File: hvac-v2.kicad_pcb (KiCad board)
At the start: 2 copper layers, 114 x 60 mm, 37 parts, among them J1 Conn_01x04, J2 Anderson_two_redblack, J3 Anderson_two_redblack, J4 Anderson_two_redblack, P1 10118194, P2 CONN_01X08, SW1 SW_SPST, SW3 KS-01Q-01, SW4 KS-01Q-01, SW5 SPST, U1 SAMD21E18, U2 WS2812b, U3 MIC5203, U4 MOSFET_CSD17318Q2, U5 WS2812b, U6 WS2812b, U7 MOSFET_CSD17318Q2, U8 DS18B20

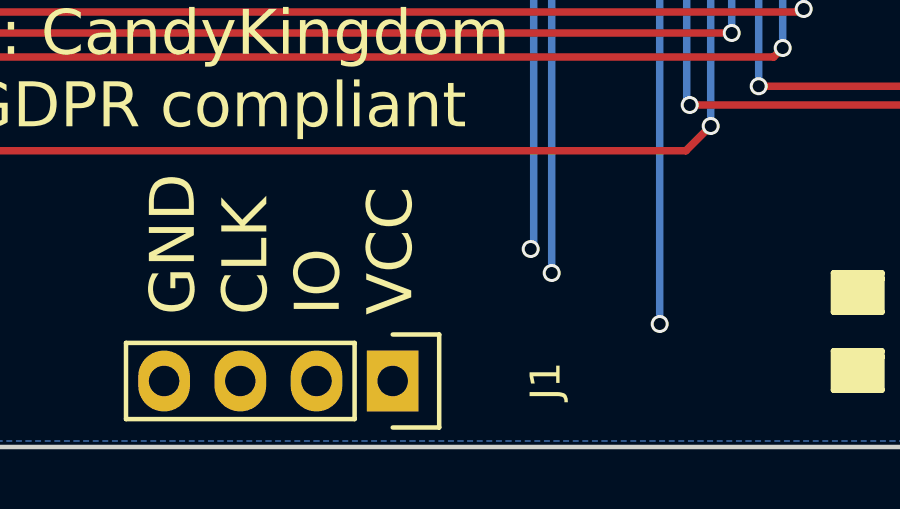
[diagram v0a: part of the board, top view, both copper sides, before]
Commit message: Connect programming headers
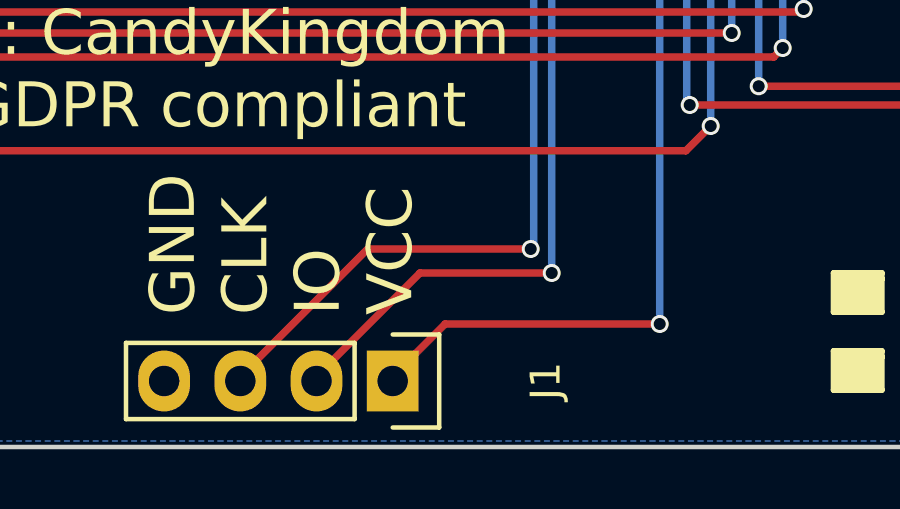
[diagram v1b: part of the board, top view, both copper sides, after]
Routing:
- net ARM_SWCLK: track 27.2 -> 38.8 mm
- net VCC: track 405.2 -> 415.0 mm
- net ARM_SWDIO: track 24.9 -> 34.3 mm
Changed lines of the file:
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@@
     (links 96)
     (no_connects 0)
-    (area 45.924999 43.924999 160.075001 104.075001)
+    (area 44.036499 35.224999 160.075001 104.075001)
     (thickness 1.6)
     (drawings 89)
-    (tracks 501)
+    (tracks 510)
     (zones 0)
     (modules 37)
@@
   (page A4)
   (layers
-    (0 F.Cu signal hide)
-    (31 B.Cu signal hide)
-    (32 B.Adhes user hide)
-    (33 F.Adhes user hide)
-    (34 B.Paste user hide)
-    (35 F.Paste user hide)
-    (36 B.SilkS user hide)
+    (0 F.Cu signal)
+    (31 B.Cu signal)
+    (32 B.Adhes user)
+    (33 F.Adhes user)
+    (34 B.Paste user)
+    (35 F.Paste user)
+    (36 B.SilkS user)
     (37 F.SilkS user)
     (38 B.Mask user)
@@
     (effects (font (size 1.5 1.5) (thickness 0.3)))
   )
-  (gr_text "TINY DIODE" (at 61.2 83.8 360) (layer F.Fab)
+  (gr_text "TINY DIODE" (at 61.2 83.8) (layer F.Fab)
     (effects (font (size 1.5 1.5) (thickness 0.3)))
   )
@@
   (segment (start 139.49 68) (end 134.89 72.6) (width 5) (layer F.Cu) (net 2))
   (segment (start 113.954002 72.6) (end 108.754002 67.4) (width 5) (layer F.Cu) (net 2))
+  (segment (start 121 99.9) (end 113.8476 99.9) (width 0.25) (layer F.Cu) (net 3))
+  (segment (start 113.8476 99.9) (end 112.1 101.6476) (width 0.25) (layer F.Cu) (net 3))
+  (segment (start 112.1 101.6476) (end 112.1 101.8) (width 0.25) (layer F.Cu) (net 3))
   (segment (start 122.275736 75.7) (end 122.7 75.7) (width 0.25) (layer F.Cu) (net 3))
   (segment (start 122.250734 75.674998) (end 122.275736 75.7) (width 0.25) (layer F.Cu) (net 3))
@@
   (segment (start 141.76 97.26) (end 141.7 97.2) (width 0.25) (layer F.Cu) (net 31))
   (via (at 141.7 97.2) (size 0.6) (drill 0.4) (layers F.Cu B.Cu) (net 31))
+  (segment (start 116.7 97.4) (end 111.2676 97.4) (width 0.25) (layer F.Cu) (net 39))
+  (segment (start 111.2676 97.4) (end 107.02 101.6476) (width 0.25) (layer F.Cu) (net 39))
+  (segment (start 107.02 101.6476) (end 107.02 101.8) (width 0.25) (layer F.Cu) (net 39))
   (segment (start 116.8 76.3) (end 116.8 97.3) (width 0.25) (layer B.Cu) (net 39))
   (segment (start 116.8 97.3) (end 116.7 97.4) (width 0.25) (layer B.Cu) (net 39))
@@
   (segment (start 116.852601 76.247399) (end 116.8 76.3) (width 0.25) (layer F.Cu) (net 39))
   (via (at 116.8 76.3) (size 0.6) (drill 0.4) (layers F.Cu B.Cu) (net 39))
+  (segment (start 117.4 98.2) (end 113.0076 98.2) (width 0.25) (layer F.Cu) (net 40))
+  (segment (start 113.0076 98.2) (end 109.56 101.6476) (width 0.25) (layer F.Cu) (net 40))
+  (segment (start 109.56 101.6476) (end 109.56 101.8) (width 0.25) (layer F.Cu) (net 40))
   (segment (start 117.5 77) (end 120.89352 77) (width 0.25) (layer F.Cu) (net 40))
   (segment (start 120.89352 77) (end 121.10092 77.2074) (width 0.25) (layer F.Cu) (net 40))

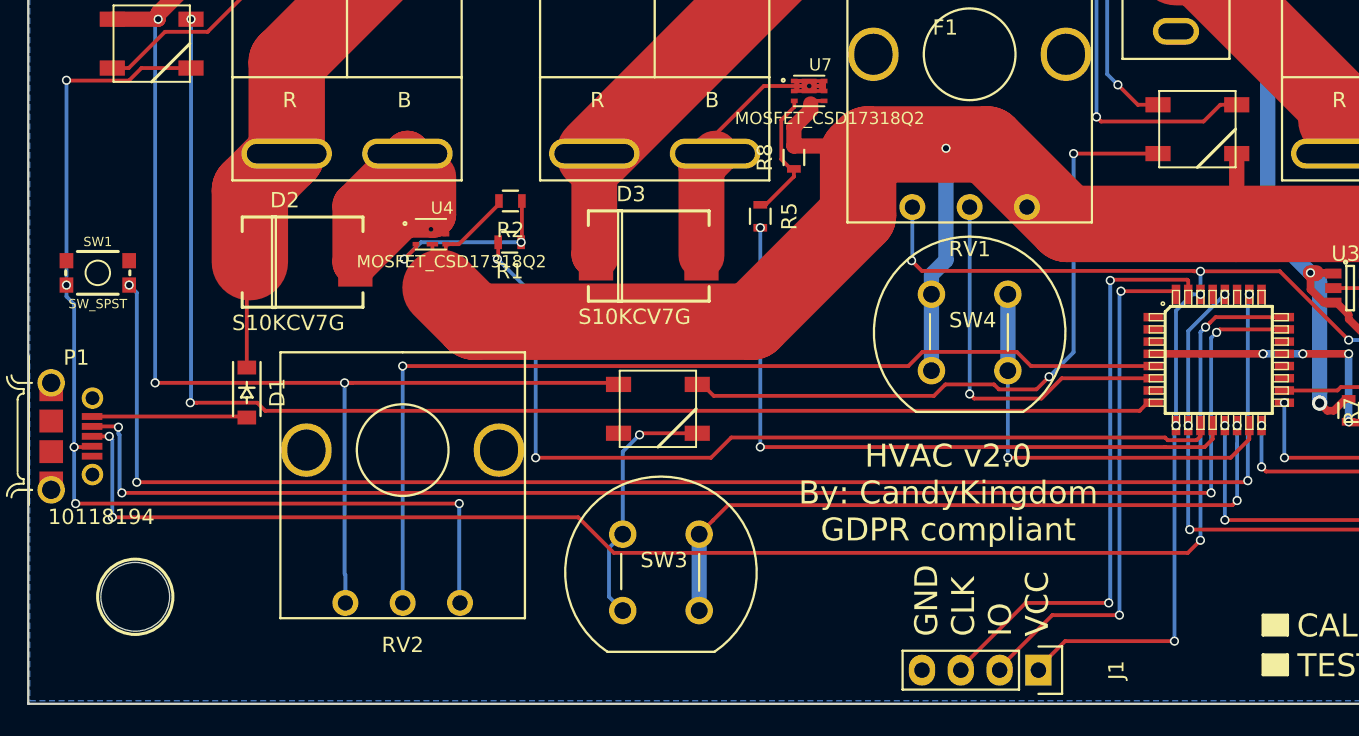
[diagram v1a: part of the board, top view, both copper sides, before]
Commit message: Hardware revision 2.1: - Fix SWD connection to power to not connect directly to VCC - Add silk labels for controls
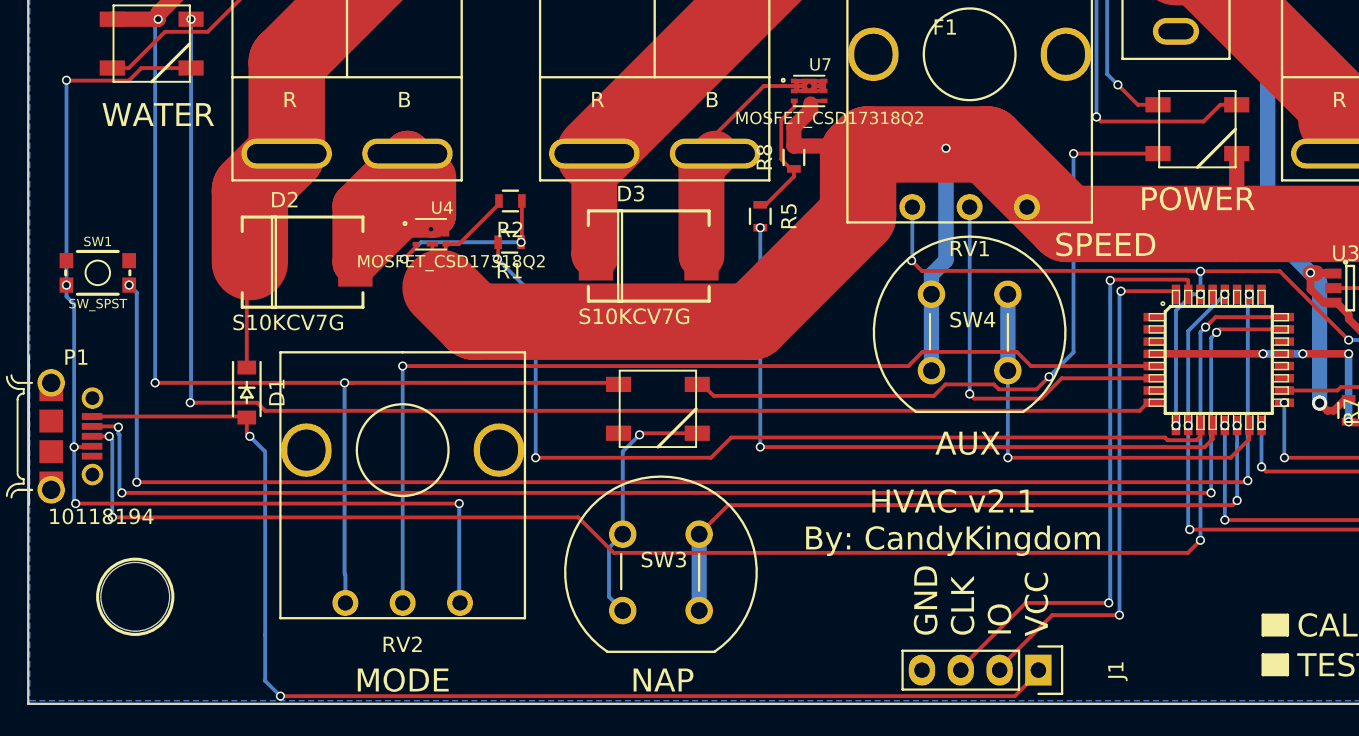
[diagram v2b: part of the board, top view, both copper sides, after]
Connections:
- D1 pad 2: Net-(D1-Pad2) -> USB_VCC
- J1 pad 1: VCC -> USB_VCC
- P1 pad 1: Net-(D1-Pad2) -> USB_VCC
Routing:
- net USB_VCC: track 0.00 -> 79.8 mm, vias 0 -> 2
- net VCC: track 415.0 -> 391.2 mm, vias 16 -> 15
- net Net-(D1-Pad2): track 10.2 -> 0.00 mm
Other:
- board text added: "AUX"
- board text added: "HVAC v2.1 By: CandyKingdom"
- board text added: "MODE"
- board text added: "NAP"
- board text added: "POWER"
- board text added: "SPEED"
- board text added: "WATER"
- board text removed: "HVAC v2.0 By: CandyKingdom GDPR compliant"

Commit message: Start placing components
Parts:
- removed P1: 10118194, 10118194-0001LF:FRAMATOME_10118194-0001LF
- removed P2: CONN_01X08, homebrew:1985250_phoenix_8pos_3.5mm
- removed RV1, RV2: POT, homebrew:BOURNS_PDB12H_POT
- removed SW3, SW4: KS-01Q-01, homebrew:BUTTON_KS-01Q-01
- removed SW5: SPST, homebrew:SWITCH_100SP1T2B3M1QEH
- removed U6: WS2812b, homebrew:WS2812B
- removed U7: MOSFET_CSD17318Q2, homebrew:TRANS_CSD17318Q2T
- removed U8: DS18B20, homebrew:TO-92
- added BZ1: Buzzer, homebrew:MURATA_PKM13EPYH4000-A0, F.Cu at (250.1, 137.4)
- added C10: 0.22uF, Capacitor_SMD:C_0805_2012Metric, F.Cu at (207.4, 189.2)
- added C11: 0.22uF, Capacitor_SMD:C_0805_2012Metric, F.Cu at (249.5, 146.0)
- added C12: 0.1uF, Capacitor_SMD:C_0402_1005Metric, F.Cu at (290.4, 148.9)
- added C13: 0.1uF, Capacitor_SMD:C_0402_1005Metric, F.Cu at (266.6, 172.8)
- added C14: 4.7uF, Capacitor_SMD:C_0603_1608Metric, F.Cu at (224.5, 190.8)
- added C15: 0.22uF, Capacitor_SMD:C_0805_2012Metric, F.Cu at (211.5, 172.8)
- added C16: 0.22uF, Capacitor_SMD:C_0805_2012Metric, F.Cu at (203.0, 189.2)
- added C17: 0.1uF, Capacitor_SMD:C_0402_1005Metric, F.Cu at (249.8, 186.7)
- added C18: 0.1uF, Capacitor_SMD:C_0402_1005Metric, F.Cu at (273.8, 165.5)
- added C19: 1000uF, Capacitor_THT:CP_Radial_D10.0mm_P5.00mm, F.Cu at (250.1, 162.4)
- added C20: 1nF, Capacitor_SMD:C_0402_1005Metric, F.Cu at (280.5, 156.1)
- added C21: 0.1uF, Capacitor_SMD:C_0402_1005Metric, F.Cu at (262.4, 175.9)
- added C22: 0.1uF, Capacitor_SMD:C_0402_1005Metric, F.Cu at (256.7, 181.8)
- added C23: 0.1uF, Capacitor_SMD:C_0402_1005Metric, F.Cu at (249.8, 188.7)
- added C24: 0.1uF, Capacitor_SMD:C_0402_1005Metric, F.Cu at (269.8, 168.9)
- added C25: 0.1uF, Capacitor_SMD:C_0402_1005Metric, F.Cu at (266.6, 170.9)
- added C26: 0.1uF, Capacitor_SMD:C_0402_1005Metric, F.Cu at (290.4, 146.9)
- added C27: 0.1uF, Capacitor_SMD:C_0402_1005Metric, F.Cu at (258.1, 178.8)
- added C28: 0.1uF, Capacitor_SMD:C_0402_1005Metric, F.Cu at (275.7, 161.6)
- added C29: 0.1uF, Capacitor_SMD:C_0402_1005Metric, F.Cu at (226.8, 157.6)
- added C30: 0.1uF, Capacitor_SMD:C_0402_1005Metric, F.Cu at (286.2, 151.9)
- added C31: 0.1uF, Capacitor_SMD:C_0402_1005Metric, F.Cu at (280.5, 158.1)
- added C32: 0.1uF, Capacitor_SMD:C_0402_1005Metric, F.Cu at (283.4, 156.1)
- added C33: 0.1uF, Capacitor_SMD:C_0402_1005Metric, F.Cu at (207.5, 172.3)
- added C34: 0.1uF, Capacitor_SMD:C_0402_1005Metric, F.Cu at (229.6, 157.6)
- added C35: 0.1uF, Capacitor_SMD:C_0402_1005Metric, F.Cu at (272.0, 131.8)
- added C36: 0.1uF, Capacitor_SMD:C_0402_1005Metric, F.Cu at (270.0, 161.6)
- added C37: 0.1uF, Capacitor_SMD:C_0402_1005Metric, F.Cu at (272.8, 161.6)
- added C38: 4.7uF, Capacitor_SMD:C_0603_1608Metric, F.Cu at (200.0, 172.6)
- added C39: 1000uF, Capacitor_THT:CP_Radial_D10.0mm_P5.00mm, F.Cu at (226.2, 183.8)
- added C4: 0.1uF, Capacitor_SMD:C_0402_1005Metric, F.Cu at (276.7, 163.5)
- added C40: 0.1uF, Capacitor_SMD:C_0402_1005Metric, F.Cu at (253.8, 181.8)
- added C41: 0.1uF, Capacitor_SMD:C_0402_1005Metric, F.Cu at (249.8, 184.8)
- added C42: 0.1uF, Capacitor_SMD:C_0402_1005Metric, F.Cu at (273.8, 163.5)
- added C43: 0.1uF, Capacitor_SMD:C_0402_1005Metric, F.Cu at (252.7, 184.8)
- added C5: 0.1uF, Capacitor_SMD:C_0402_1005Metric, F.Cu at (294.4, 144.0)
- added C6: 0.1uF, Capacitor_SMD:C_0402_1005Metric, F.Cu at (252.7, 186.7)
- added C7: 0.1uF, Capacitor_SMD:C_0402_1005Metric, F.Cu at (278.6, 160.8)
- added C8: 0.1uF, Capacitor_SMD:C_0402_1005Metric, F.Cu at (260.9, 178.8)
- added C9: 4.7uF, Capacitor_SMD:C_0603_1608Metric, F.Cu at (254.1, 155.2)
- added D10: TVS_5V, Diode_SMD:D_SOD-323, F.Cu at (254.8, 172.6)
- added D11: TVS_5V, Diode_SMD:D_SOD-323, F.Cu at (282.9, 146.1)
- added D12: TVS_5V, Diode_SMD:D_SOD-323, F.Cu at (254.8, 169.7)
- added D13: TVS_5V, Diode_SMD:D_SOD-323, F.Cu at (236.6, 188.1)
- added D14: TVS_5V, Diode_SMD:D_SOD-323, F.Cu at (293.6, 130.6)
- added D15: TVS_5V, Diode_SMD:D_SOD-323, F.Cu at (254.3, 149.5)
- added D16: D_Schottky, Diode_THT:D_DO-201AD_P12.70mm_Horizontal, F.Cu at (218.1, 162.3)
- added D17: D_Schottky, Diode_THT:D_DO-201AD_P12.70mm_Horizontal, F.Cu at (194.2, 184.1)
- added D18: D_Schottky, Diode_THT:D_DO-201AD_P12.70mm_Horizontal, F.Cu at (227.7, 146.1)
- added D19: TVS_5V, Diode_SMD:D_SOD-323, F.Cu at (216.1, 189.2)
- added D20: TVS_5V, Diode_SMD:D_SOD-323, F.Cu at (246.5, 179.8)
- added D21: TVS_5V, Diode_SMD:D_SOD-323, F.Cu at (294.2, 133.6)
- added D22: TVS_5V, Diode_SMD:D_SOD-323, F.Cu at (240.9, 188.1)
- added D23: TVS_5V, Diode_SMD:D_SOD-323, F.Cu at (220.4, 189.2)
- added D24: TVS_5V, Diode_SMD:D_SOD-323, F.Cu at (254.3, 152.4)
- added D4: TVS_12V, Diode_SMD:D_SMB_Handsoldering, F.Cu at (292.5, 126.3)
- added D5: LED, LED_SMD:LED_0805_2012Metric, F.Cu at (211.5, 175.9)
- added D6: TVS_5V, Diode_SMD:D_SOD-323, F.Cu at (294.2, 136.5)
- added D7: TVS_5V, Diode_SMD:D_SOD-323, F.Cu at (259.1, 171.3)
- added D8: D_Schottky, Diode_THT:D_DO-201AD_P12.70mm_Horizontal, F.Cu at (171.5, 62.6)
- added D9: D_Schottky, Diode_THT:D_DO-201AD_P12.70mm_Horizontal, F.Cu at (171.5, 56.3)
- added J10: Conn_01x02, Connector_PinHeader_2.54mm:PinHeader_1x02_P2.54mm_Horizontal, F.Cu at (90.1, 97.6)
- added J11: Conn_01x03, Connector_PinHeader_2.54mm:PinHeader_1x03_P2.54mm_Horizontal, F.Cu at (89.9, 78.1)
- added J12: Conn_01x03, Connector_PinHeader_2.54mm:PinHeader_1x03_P2.54mm_Horizontal, F.Cu at (90.1, 89.4)
- added J13: Conn_01x03, Connector_PinHeader_2.54mm:PinHeader_1x03_P2.54mm_Horizontal, F.Cu at (90.0, 118.0)
- added J14: Conn_01x04, Connector_PinHeader_2.54mm:PinHeader_1x04_P2.54mm_Horizontal, F.Cu at (259.5, 142.8)
- added J5: Conn_01x03, Connector_PinHeader_2.54mm:PinHeader_1x03_P2.54mm_Horizontal, F.Cu at (89.9, 107.4)
- added J6: Conn_01x03, Connector_PinHeader_2.54mm:PinHeader_1x03_P2.54mm_Horizontal, F.Cu at (259.5, 133.1)
- added J7: Anderson_two_redblack_sink, homebrew:Anderson_1336G1_right_angle_bottom_two, F.Cu at (114.1, 51.1)
- added J8: Anderson_two_redblack_sink, homebrew:Anderson_1336G1_right_angle_bottom_two, F.Cu at (93.8, 51.4)
- added J9: Conn_01x02, Connector_PinHeader_2.54mm:PinHeader_1x02_P2.54mm_Horizontal, F.Cu at (90.1, 67.0)
- added JP1: SolderJumper_2_Open, Jumper:SolderJumper-2_P1.3mm_Open_TrianglePad1.0x1.5mm, F.Cu at (254.3, 146.2)
- added JP2: SolderJumper_2_Open, Jumper:SolderJumper-2_P1.3mm_Open_TrianglePad1.0x1.5mm, F.Cu at (211.8, 189.4)
- added Q1: AO3400A, Package_TO_SOT_SMD:SOT-23, F.Cu at (245.0, 146.8)
- added Q2: AO3400A, Package_TO_SOT_SMD:SOT-23, F.Cu at (198.5, 189.8)
- added Q3: AO3400A, Package_TO_SOT_SMD:SOT-23, F.Cu at (194.1, 189.8)
- added R10: 10k, Resistor_SMD:R_0603_1608Metric, F.Cu at (232.5, 190.8)
- added R11: 10k, Resistor_SMD:R_0603_1608Metric, F.Cu at (294.1, 139.2)
- added R12: 10k, Resistor_SMD:R_0603_1608Metric, F.Cu at (263.2, 171.1)
- added R13: 150, Resistor_SMD:R_0603_1608Metric, F.Cu at (287.0, 144.7)
- added R14: 470, Resistor_SMD:R_0603_1608Metric, F.Cu at (282.7, 148.8)
- added R15: 150, Resistor_SMD:R_0603_1608Metric, F.Cu at (277.1, 156.0)
- added R16: 47, Resistor_SMD:R_0603_1608Metric, F.Cu at (282.7, 151.3)
- added R17: 10k, Resistor_SMD:R_0603_1608Metric, F.Cu at (287.0, 147.2)
- added R18: 10k, Resistor_SMD:R_0603_1608Metric, F.Cu at (270.4, 166.6)
- added R19: 10k, Resistor_SMD:R_0603_1608Metric, F.Cu at (240.5, 190.8)
- added R20: 10k, Resistor_SMD:R_0603_1608Metric, F.Cu at (291.0, 144.7)
- added R21: 24k, Resistor_SMD:R_0603_1608Metric, F.Cu at (246.3, 187.6)
- added R22: 24k, Resistor_SMD:R_0603_1608Metric, F.Cu at (254.6, 179.6)
- added R23: 150, Resistor_SMD:R_0603_1608Metric, F.Cu at (246.3, 185.0)
- added R24: 150, Resistor_SMD:R_0603_1608Metric, F.Cu at (250.4, 182.5)
- added R25: 4k7, Resistor_SMD:R_0603_1608Metric, F.Cu at (270.4, 164.1)
- added R26: 4k7, Resistor_SMD:R_0603_1608Metric, F.Cu at (246.3, 182.5)
- added R27: 4k7, Resistor_SMD:R_0603_1608Metric, F.Cu at (286.7, 149.7)
- added R28: 4k7, Resistor_SMD:R_0603_1608Metric, F.Cu at (282.7, 153.8)
- added R3: 10k, Resistor_SMD:R_0603_1608Metric, F.Cu at (244.5, 190.8)
- added R4: 10k, Resistor_SMD:R_0603_1608Metric, F.Cu at (228.5, 190.8)
- added R9: 110k, Resistor_SMD:R_0603_1608Metric, F.Cu at (250.6, 179.6)
- added SW2: Rotary_Encoder_Switch, homebrew:BOURNS_PEC12R-4xxxF-Sxxxx, F.Cu at (183.8, 182.9)
- C1: value 10uF -> 4.7uF; footprint Capacitors_SMD:C_0805 -> Capacitor_SMD:C_0603_1608Metric
- C2: value 1uF -> 0.1uF; footprint Capacitors_SMD:C_0603 -> Capacitor_SMD:C_0402_1005Metric
- C3: value 1uF -> 1nF; footprint Capacitors_SMD:C_0603 -> Capacitor_SMD:C_0402_1005Metric
- D1: value BAT54GWJ -> TVS_5V; footprint Diodes_SMD:SOD-123 -> Diode_SMD:D_SOD-323
- D2: value S10KCV7G -> TVS_5V; footprint homebrew:DIODE-DO-214AB -> Diode_SMD:D_SOD-323
- D3: value S10KCV7G -> D_Schottky; footprint homebrew:DIODE-DO-214AB -> Diode_THT:D_DO-201AD_P12.70mm_Horizontal
- F1: footprint homebrew:FUSEHOLDER_ATC_Bk-6010 -> homebrew:FUSE_3550-2
- J1: value Conn_01x04 -> Anderson_two_redblack; footprint Pin_Headers:Pin_Header_Straight_1x04 -> homebrew:Anderson_1336G1_right_angle_bottom_two
- J2: value Anderson_two_redblack -> Conn_01x04; footprint homebrew:Anderson_1337G3_right_angle_bottom_two -> Connector_PinHeader_2.54mm:PinHeader_1x04_P2.54mm_Horizontal
- J3: value Anderson_two_redblack -> Conn_01x02; footprint homebrew:Anderson_1337G3_right_angle_bottom_two -> Connector_PinHeader_2.54mm:PinHeader_1x02_P2.54mm_Horizontal
- J4: value Anderson_two_redblack -> Anderson_two_redblack_src; footprint homebrew:Anderson_1337G3_right_angle_bottom_two -> homebrew:Anderson_1336G1_right_angle_bottom_two
- R1: footprint Resistors_SMD:R_0603 -> Resistor_SMD:R_0603_1608Metric
- R2: value 10k -> 24k; footprint Resistors_SMD:R_0603 -> Resistor_SMD:R_0603_1608Metric
- R5: value 470 -> 10k; footprint Resistors_SMD:R_0603 -> Resistor_SMD:R_0603_1608Metric
- R6: value 33k -> 24k; footprint Resistors_SMD:R_0603 -> Resistor_SMD:R_0603_1608Metric
- R7: value 10k -> 150; footprint Resistors_SMD:R_0603 -> Resistor_SMD:R_0603_1608Metric
- R8: value 10k -> 390k; footprint Resistors_SMD:R_0603 -> Resistor_SMD:R_0603_1608Metric
- SW1: value SW_SPST -> SW_Push; footprint Sparkfun-Switches:TACTILE_SWITCH_SMD_4.6X2.8MM -> homebrew:SW_TACTILE_5.1MM_TS-1187A-C-D-B
- U1: value SAMD21E18 -> STM32F030C8Tx; footprint homebrew:TQFP32-08 -> Package_QFP:LQFP-48_7x7mm_P0.5mm
- U2: value WS2812b -> IFX007T; footprint homebrew:WS2812B -> Package_TO_SOT_SMD:TO-263-7_TabPin8
- U3: value MIC5203 -> IFX007T; footprint TO_SOT_Packages_SMD:SOT-23-5 -> Package_TO_SOT_SMD:TO-263-7_TabPin8
- U4: value MOSFET_CSD17318Q2 -> AMS1117-3.3; footprint homebrew:TRANS_CSD17318Q2T -> Package_TO_SOT_SMD:SOT-223-3_TabPin2
- U5: value WS2812b -> DS18B20; footprint homebrew:WS2812B -> Package_TO_SOT_THT:TO-92_Inline
- moved H2 243.1 mm to (275.6, 149.7)
- moved D1 233.9 mm to (289.4, 130.6), turned to 0 degrees
- moved SW1 231.3 mm to (263.4, 166.4)
- moved R1 227.0 mm to (294.1, 141.7), turned to 0 degrees
- moved H3 219.1 mm to (263.5, 157.8)
- moved D2 215.7 mm to (254.8, 175.6)
- moved R2 209.8 mm to (258.9, 176.6), turned to 0 degrees
- moved U4 199.6 mm to (239.4, 182.4)
- moved R5 197.4 mm to (263.2, 173.6), turned to 0 degrees
- moved U2 192.9 mm to (234.2, 129.8)
- moved R8 186.4 mm to (236.5, 190.8), turned to 0 degrees
- moved J3 181.3 mm to (227.7, 151.8)
- moved U5 174.1 mm to (270.5, 158.0)
- moved C3 170.6 mm to (293.3, 146.9), turned to 0 degrees
- moved C2 165.3 mm to (286.2, 153.9), turned to 0 degrees
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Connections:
- C1 pad 1: +BATT -> VCC
- C2 pad 1: +BATT -> /NRST
- C3 pad 1: VCC -> /BRIDGE_SENSE_P
- D1 pad 1: +BATT -> /FAN_SENSE
- D1 pad 2: USB_VCC -> GND
- D2 pad 1: +BATT -> /VBATT_DIV
- D2 pad 2: FAN_OUT -> GND
- D3 pad 1: +BATT -> /FAN_P
- D3 pad 2: PUMP_OUT -> /FAN_N
- F1 pad 1: Net-(F1-Pad1) -> Net-(D8-Pad1)
- J1 pad 1: USB_VCC -> /FAN_P
- J1 pad 2: ARM_SWDIO -> /FAN_N
- J2 pad 1: Net-(J2-Pad1) -> /SCL
- J2 pad 2: GND -> /SDA
- J3 pad 1: +BATT -> Net-(D6-Pad2)
- J3 pad 2: FAN_OUT -> GND
- J4 pad 1: +BATT -> Net-(D8-Pad1)
- J4 pad 2: PUMP_OUT -> GND
- R1 pad 1: Net-(R1-Pad1) -> /BRIDGE_SENSE_P
- R1 pad 2: FAN_SIGNAL -> GND
- R2 pad 1: Net-(R1-Pad1) -> /BOOT0
- R5 pad 1: Net-(R5-Pad1) -> Net-(C7-Pad2)
- R5 pad 2: PUMP_SIGNAL -> GND
- R6 pad 1: +BATT -> Net-(JP2-Pad1)
- R6 pad 2: VBATT_DIV -> /FAN_SENSE
- R7 pad 1: VBATT_DIV -> Net-(Q1-Pad1)
- R7 pad 2: GND -> /FAN_SIGNAL
- R8 pad 1: Net-(R5-Pad1) -> +BATT
- R8 pad 2: GND -> /VBATT_DIV
- SW1 pad 1: GND -> /NRST
- SW1 pad 2: Net-(SW1-Pad2) -> GND
- U1 pad 1: Net-(U1-Pad1) -> VCC
- U1 pad 10: GND -> /VBATT_DIV
- U1 pad 11: FAN_SIGNAL -> /PUMP_SENSE
- U1 pad 12: PUMP_SIGNAL -> /BRIDGE_SENSE_P
- U1 pad 13: FAN_PWM -> /BRIDGE_SENSE_N
- U1 pad 14: NAP_BUTTON -> /VBATT_DIV
- U1 pad 15: AUX_BUTTON -> /PUMP_SENSE
- U1 pad 16: INTERNAL_TEMP -> /FAN_SENSE
- U1 pad 17: EXTERNAL_TEMP -> /ACC_SENSE
- U1 pad 18: FLOAT_SWITCH -> /BRIDGE_ENABLE
- U1 pad 19: Net-(U1-Pad19) -> /BUZZER
- U1 pad 2: Net-(U1-Pad2) -> (no net)
- U1 pad 20: Net-(U1-Pad20) -> /BRIDGE_N
- U1 pad 21: Net-(U1-Pad21) -> (no net)
- U1 pad 22: Net-(U1-Pad22) -> (no net)
- U1 pad 23: USB_D- -> GND
- U1 pad 24: USB_D+ -> VCC
- U1 pad 25: Net-(U1-Pad25) -> (no net)
- U1 pad 26: Net-(SW1-Pad2) -> (no net)
- U1 pad 27: Net-(U1-Pad27) -> /ENC_A
- U1 pad 28: GND -> /ENC_B
- U1 pad 29: Net-(U1-Pad29) -> /PWM_OUT
- U1 pad 3: Net-(U1-Pad3) -> (no net)
- U1 pad 30: VCC -> /FAN_SIGNAL
- U1 pad 31: ARM_SWCLK -> /PUMP_SIGNAL
- U1 pad 32: ARM_SWDIO -> /LED
- U1 pad 4: VBATT_DIV -> (no net)
- U1 pad 5: MODE -> /SDA
- U1 pad 6: SPEED -> /SCL
- U1 pad 7: Net-(U1-Pad7) -> /NRST
- U1 pad 8: LED -> GND
- U2 pad 1: VCC -> GND
- U2 pad 2: Net-(U2-Pad2) -> Net-(R3-Pad2)
- U2 pad 3: GND -> Net-(R4-Pad2)
- U2 pad 4: LED -> /FAN_P
- U3 pad 1: +BATT -> GND
- U3 pad 2: GND -> Net-(R12-Pad1)
- U3 pad 3: +BATT -> Net-(R11-Pad1)
- U3 pad 4: Net-(U3-Pad4) -> /FAN_N
- U3 pad 5: VCC -> Net-(C18-Pad1)
- U4 pad 2: Net-(R1-Pad1) -> VCC
- U4 pad 3: FAN_OUT -> +BATT
- U5 pad 1: VCC -> GND
- U5 pad 2: Net-(U5-Pad2) -> /TEMP_BUILTIN
- U5 pad 3: GND -> VCC
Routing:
- net VCC: track 391.2 -> 0.00 mm, vias 15 -> 0
- net GND: track 301.6 -> 0.00 mm, vias 16 -> 0
- net +BATT: track 190.2 -> 0.00 mm, vias 3 -> 0
- net USB_D+: track 98.5 -> 0.00 mm, vias 4 -> 0
- net Net-(SW1-Pad2): track 98.1 -> 0.00 mm, vias 4 -> 0
- net Net-(U2-Pad2): track 94.9 -> 0.00 mm, vias 4 -> 0
- net USB_D-: track 92.6 -> 0.00 mm, vias 4 -> 0
- net LED: track 88.6 -> 0.00 mm, vias 2 -> 0
- net USB_VCC: track 79.8 -> 0.00 mm, vias 2 -> 0
- net MODE: track 65.4 -> 0.00 mm, vias 1 -> 0
- net FAN_SIGNAL: track 60.1 -> 0.00 mm, vias 2 -> 0
- net EXTERNAL_TEMP: track 48.1 -> 0.00 mm, vias 3 -> 0
- net Net-(J2-Pad1): track 47.5 -> 0.00 mm
- net FAN_PWM: track 47.0 -> 0.00 mm, vias 3 -> 0
- net NAP_BUTTON: track 46.7 -> 0.00 mm, vias 2 -> 0
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- removed copper zone on B.Cu, net GND
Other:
- board outline removed
- board text added: "20A MAX"
- board text added: "hvac-v2.2"
- board text removed: "AUX"
- board text removed: "BIG DIODE"
- board text removed: "BUTTON"
- board text removed: "CAL"
- board text removed: "CPU"
- board text removed: "F"
- board text removed: "FAN"
- board text removed: "FUSE"
- board text removed: "G"
- board text removed: "GND CLK IO VCC"
- board text removed: "HVAC v2.1 By: CandyKingdom"
- board text removed: "IN"
- board text removed: "LED"
- board text removed: "MODE"
- board text removed: "MOSFET"
- board text removed: "NAP"
- board text removed: "POWER"
- board text removed: "POWER_SW"
- board text removed: "PUMP"
- board text removed: "SPEED"
- board text removed: "T"
- board text removed: "TEMP PROBE"
- board text removed: "TEST"
- board text removed: "TINY DIODE"
- board text removed: "V"
- board text removed: "V: VCC T: EXTERNAL TEMP G: GROUND F: FAN W: WATER SWITCH"
- board text removed: "W"
- board text removed: "WATER"

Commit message: Component placement finished
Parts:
- added H5: HOLE, homebrew:HOLE_M4, F.Cu at (117.4, 93.9)
- added R29: 110k, Resistor_SMD:R_0603_1608Metric, F.Cu at (106.1, 115.3)
- added R30: 10k, Resistor_SMD:R_0603_1608Metric, F.Cu at (77.3, 135.2)
- added R31: 110k, Resistor_SMD:R_0603_1608Metric, F.Cu at (72.7, 112.9)
- added R32: 10k, Resistor_SMD:R_0603_1608Metric, F.Cu at (110.2, 119.5)
- added R33: 10k, Resistor_SMD:R_0603_1608Metric, F.Cu at (126.9, 121.1)
- added R34: 150, Resistor_SMD:R_0603_1608Metric, F.Cu at (143.9, 116.9)
- added R35: 150, Resistor_SMD:R_0603_1608Metric, F.Cu at (144.6, 125.6)
- added R36: 150, Resistor_SMD:R_0603_1608Metric, F.Cu at (143.8, 109.7)
- added R37: 150, Resistor_SMD:R_0603_1608Metric, F.Cu at (143.8, 102.6)
- J2: moved to B.Cu
- moved H4 254.3 mm to (35.0, 104.0)
- moved R11 226.1 mm to (69.5, 112.9)
- moved C30 224.0 mm to (65.6, 113.0), turned to 90 degrees
- moved D4 222.8 mm to (69.8, 132.0), turned to 180 degrees
- moved D21 220.8 mm to (74.6, 110.5), turned to 270 degrees
- moved R14 219.4 mm to (64.6, 125.5), turned to 180 degrees
- moved C20 217.7 mm to (64.7, 127.0), turned to 180 degrees
- moved C19 215.7 mm to (35.7, 138.9), turned to 90 degrees
- moved H1 214.2 mm to (35.0, 147.0)
- moved C18 213.1 mm to (65.2, 122.3), turned to 180 degrees
- moved C35 206.8 mm to (67.1, 103.6), turned to 180 degrees
- moved C12 206.3 mm to (85.6, 124.2), turned to 270 degrees
- moved R1 205.1 mm to (91.1, 112.2), turned to 90 degrees
- moved C13 205.0 mm to (66.7, 127.3), turned to 90 degrees
- moved C3 203.8 mm to (92.5, 112.0), turned to 90 degrees
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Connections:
- C28 pad 1: /SW_2 -> Net-(C28-Pad1)
- C29 pad 1: /SW_3 -> Net-(C29-Pad1)
- C31 pad 1: /SW_WATER -> Net-(C31-Pad1)
- C32 pad 1: /SW_1 -> Net-(C32-Pad1)
- D14 pad 1: /SW_2 -> Net-(C28-Pad1)
- D15 pad 1: /SW_3 -> Net-(C29-Pad1)
- D19 pad 1: /SW_WATER -> Net-(C31-Pad1)
- D20 pad 1: /SW_1 -> Net-(C32-Pad1)
- J10 pad 2: /SW_1 -> Net-(C32-Pad1)
- J5 pad 2: /SW_2 -> Net-(C28-Pad1)
- J6 pad 2: /SW_3 -> Net-(C29-Pad1)
- J9 pad 2: /SW_WATER -> Net-(C31-Pad1)
- U1 pad 21: (no net) -> /SW_WATER
- U1 pad 22: (no net) -> /SW_1
- U1 pad 25: (no net) -> /SW_2
- U1 pad 26: (no net) -> /SW_3
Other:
- board outline added: 125 x 93 mm

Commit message: Start routing
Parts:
- added H6: SLOT, homebrew:SLOT_W2mm_H8mm, F.Cu at (142.1, 138.8)
- F1: value BK-6010 -> ATC
- moved R30 58.8 mm to (133.4, 117.6)
- moved R7 58.8 mm to (131.7, 117.6)
- moved C19 31.9 mm to (54.4, 113.0), turned to 180 degrees
- moved C13 10.0 mm to (64.1, 117.6)
- moved C12 7.89 mm to (84.4, 116.4), turned to 90 degrees
- moved R25 4.60 mm to (145.0, 135.0), turned to 180 degrees
- moved C20 3.00 mm to (62.3, 125.2), turned to 90 degrees
- moved C40 2.53 mm to (146.2, 141.6)
- moved U5 1.80 mm to (144.9, 138.9)
- moved JP1 1.20 mm to (103.0, 129.9), turned to 270 degrees
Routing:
- net +BATT: track 0.00 -> 240.1 mm
- net GND: track 0.00 -> 232.2 mm, vias 0 -> 6
- net VCC: track 0.00 -> 78.8 mm, vias 0 -> 8
- net /FAN_P: track 0.00 -> 53.8 mm
- net /FAN_N: track 0.00 -> 46.8 mm
- net Net-(D8-Pad1): track 0.00 -> 38.9 mm
- net /PUMP_OUT: track 0.00 -> 19.0 mm
- net /ACC_OUT: track 0.00 -> 19.0 mm
- net Net-(JP2-Pad1): track 0.00 -> 2.97 mm
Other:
- outline, holes or cut-outs redrawn
